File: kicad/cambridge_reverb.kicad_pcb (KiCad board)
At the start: 2 copper layers, 190 x 115 mm, 178 parts, among them IC1 TL072CP, IC2 TL072CP, IC3 TL074CN, Q1 MMBF5457, Q2 MMBF5457, T1 reuse / AnTek AS-0524, U1 LM317T

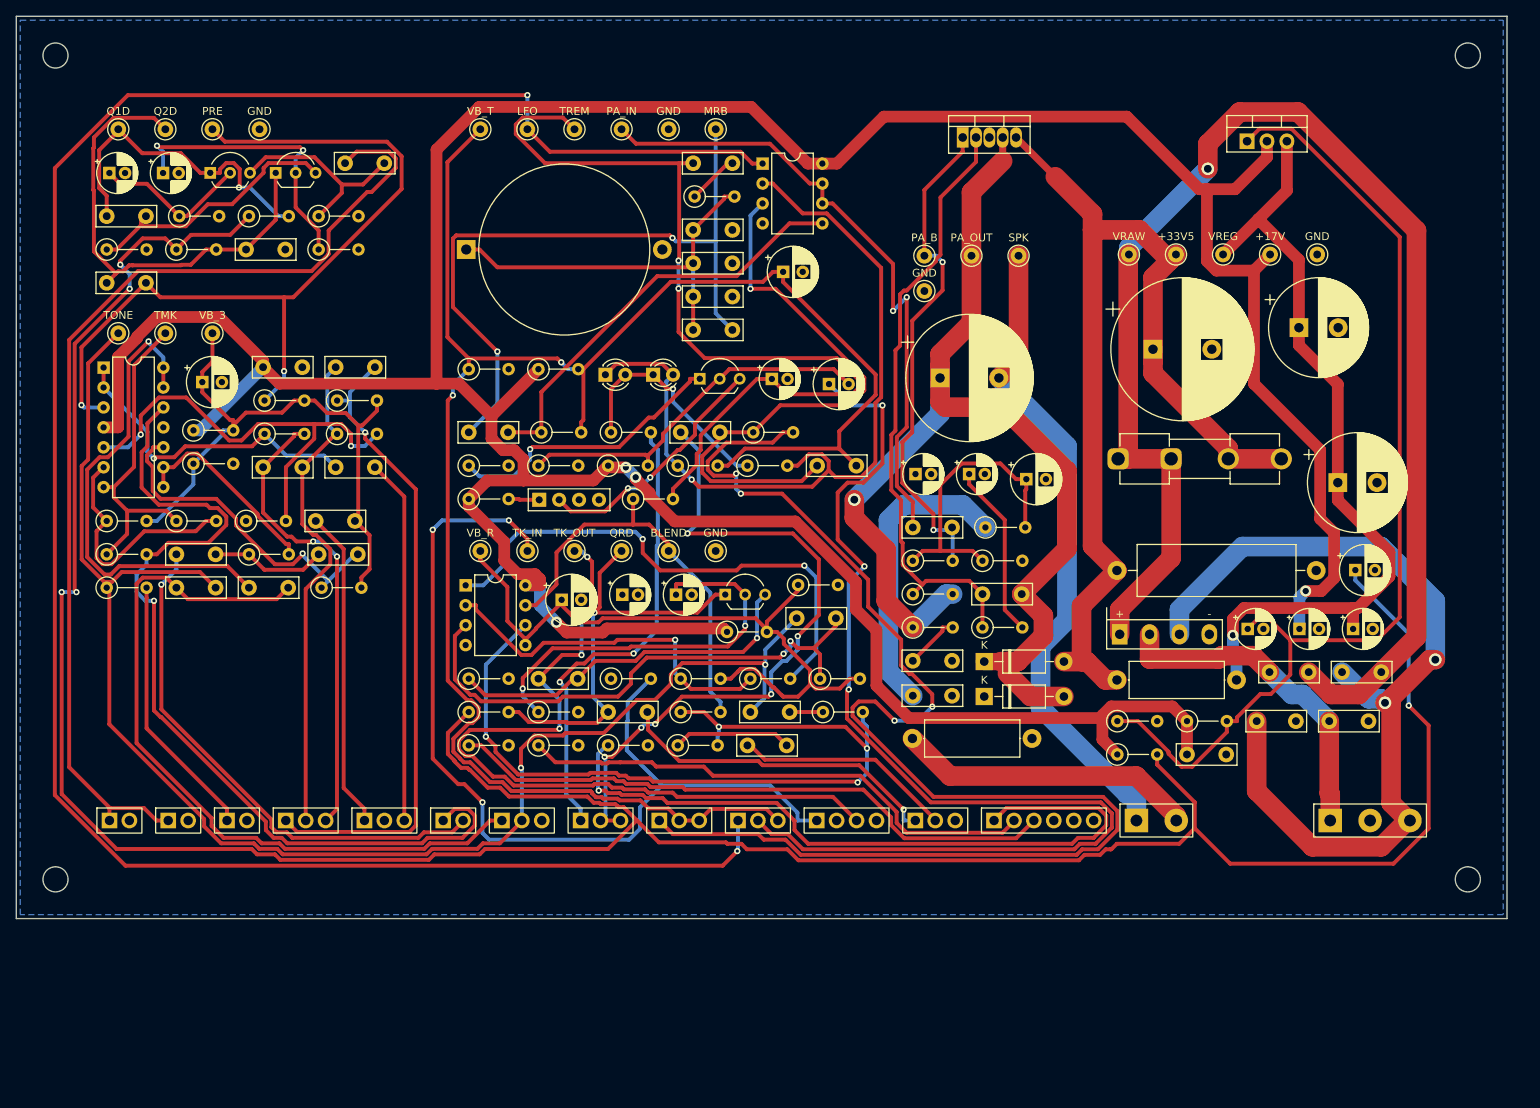
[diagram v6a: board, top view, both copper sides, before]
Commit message: Four-layer boards, no routes through footprints, rules by impedance, RF stoppers
Both boards move to a 4-layer stack (JLC04161H-7628): F.Cu signal, In1 solid GND
plane, In2 inner signal layer, B.Cu signal + shield-only GND pour, locked perimeter
GND stitching vias every 15 mm. Outer traces sit 0.21 mm from the plane instead of
1.5 mm; the long runs live on In2 under the plane and the outer layers carry escapes.

- No routes through footprints: gen_pcb writes keepout rule areas (kp_<ref>, tracks;
  vias too under SMD parts; component side) between every part's pads -- pin-to-pin
  strips and the body between rows -- with same-net pin gaps exempt and power-only
  parts exempt. 155 / 147 areas. Freerouting gets them as keepouts, KiCad DRC checks.
- Rules by impedance: new HiZ net class (0.3 mm; gates, RF nodes, tone ladder and
  wipers, LFO timing, MRB tank, PA + input), Default = low-Z signal, Power 1.0 mm,
  HighCurrent 1.5 mm, TankDrive; .kicad_dru: HighCurrent >= 0.6 mm from any signal
  trace, tank drive >= 0.8 mm from the return (SMD 0.4 / 0.6), tracks and vias only;
  route_board hands the router the same per-class clearances.
- RF stoppers R_rf1/C_rf1 (1k + 100 pF) at Q1's gate and R_rf2/C_rf2 at the recovery
  JFET's gate (the guitar and tank cables are the antennas). Noise floor unchanged.
- route_board: strips the plane layer from the DSN (Freerouting 1.9 ignores
  (active off) and routed 7 m of copper on the planes; typed as a power layer it
  treated every through-hole pad as connected), routes inner signal layers, per-board
  class clearances, 4-layer defaults.
- SMD board 170x100 mm, 1.2 mm gap (was 155x90 / 0.5): with the keepouts every SMD
  ground / rail pad needs a via beside it and none fitted; smaller SMD rail vias.
  THT gap 1.6 mm. Placer: gaps are the routing channels now.
- Crosstalk audit knows the 4-layer geometry; cost model notes the 4-layer PCB.

Routing: THT 218/226, 0 DRC errors, 0 rule hits; SMD 216/226, 1 starved thermal.
Crosstalk aft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
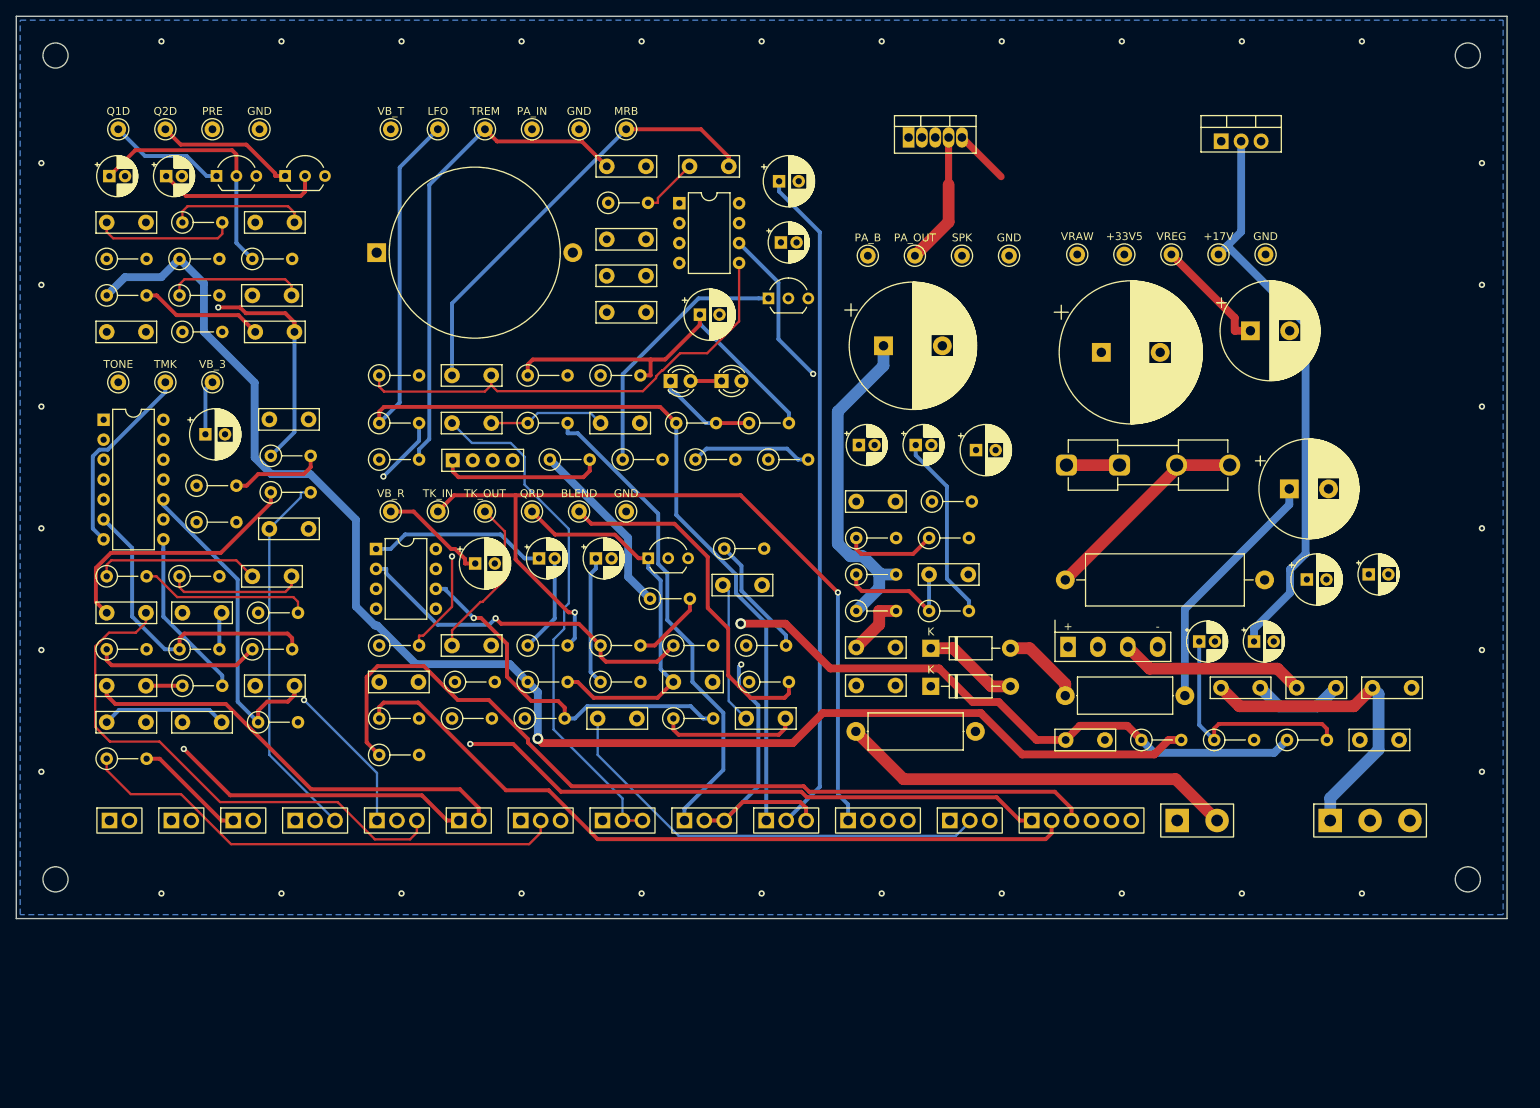
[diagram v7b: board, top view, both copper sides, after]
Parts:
- added C_rf1: 100pF, C_Disc_D7.5mm_W2.5mm_P5.00mm, F.Cu at (11.5, 26.3)
- added C_rf2: 100pF, C_Disc_D7.5mm_W2.5mm_P5.00mm, F.Cu at (46.3, 84.8)
- added R_rf1: 1k, R_Axial_DIN0207_L6.3mm_D2.5mm_P5.08mm_Vertical, F.Cu at (21.2, 26.3)
- added R_rf2: 1k, R_Axial_DIN0207_L6.3mm_D2.5mm_P5.08mm_Vertical, F.Cu at (46.3, 80.2)
- moved C_j3 34.6 mm to (11.5, 76.0)
- moved R_j3 34.5 mm to (11.5, 71.4)
- moved R_trem1 32.8 mm to (46.3, 56.5)
- moved R_j2 30.1 mm to (20.8, 71.4)
- moved R_lfo_ser 29.6 mm to (46.3, 51.8)
- moved C_lfo1 29.2 mm to (55.5, 51.8)
- moved R_lfo_sh 28.8 mm to (65.2, 51.8)
- moved C_j2 28.7 mm to (30.1, 71.4)
- moved C_lfo2 28.1 mm to (74.5, 51.8)
- moved R_g1 27.6 mm to (11.5, 30.9)
- moved C_drv 26.6 mm to (97.2, 21.0)
- moved R_obuf_b 21.9 mm to (46.3, 45.8)
- moved R_fx_pad 21.8 mm to (11.5, 94.6)
- moved C_cpl12 21.1 mm to (30.1, 35.6)
- moved C_mrb_out 20.9 mm to (85.8, 19.1)
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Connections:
- C_in_pre pad 2: Q1G -> RF1
- C_rev2 pad 2: QRG -> RF2
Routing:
- net +17V_PRE: track 362.8 -> 217.1 mm, vias 5 -> 1
- net +17V: track 493.1 -> 358.3 mm, vias 4 -> 1
- net LFO_OUT: track 305.0 -> 170.3 mm, vias 3 -> 0
- net SPD_B: track 176.8 -> 61.7 mm, vias 4 -> 0
- net VOLTOP: track 95.9 -> 16.0 mm
- net VBIAS_T: track 235.9 -> 162.7 mm, vias 2 -> 1
- net VRAW: track 180.5 -> 111.2 mm, vias 1 -> 0
- net AC2: track 114.2 -> 47.4 mm, vias 2 -> 0
- net LFO_N: track 102.7 -> 40.5 mm, vias 1 -> 0
- net DPT_W: track 142.1 -> 85.4 mm, vias 3 -> 0
- net SUMJ: track 104.5 -> 54.1 mm, vias 4 -> 1
- net JWT: track 0.00 -> 48.0 mm
- net PA_OUT: track 146.5 -> 104.2 mm, vias 1 -> 0
- net PA_IN: track 82.4 -> 41.7 mm, vias 2 -> 1
- net +33V5: track 169.2 -> 132.6 mm
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- added copper zone on In1.Cu, net GND
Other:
- copper layers 2 -> 4
